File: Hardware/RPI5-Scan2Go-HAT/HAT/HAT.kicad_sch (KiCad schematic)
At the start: 30 parts, among them J1 RPi_GPIO, J10 Conn_01x02_Socket, J12 Conn_01x02_Socket, J13 Conn_01x02_Socket, J14 Conn_01x02_Socket, J15 Jack-DC 5V, J18 Conn_01x02_Socket, J19 Conn_01x02_Socket, J2 Conn_01x04_Socket, J20 Conn_01x05_Socket, J21 Conn_01x05_Socket, J22 Conn_01x02_Socket, J23 Conn_01x04_Socket, J24 Conn_01x02_Socket, J3 Conn_01x14_Socket, J4 Conn_01x03_Socket, J5 Conn_01x03_Socket, J6 Conn_01x03_Socket, J7 Conn_01x04_Socket, J8 Conn_01x02_Socket, J9 Conn_01x02_Socket, Q1 DMG2305UX, U1 Pico

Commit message: improved layout
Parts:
- renumbered J3 to J1, J24 to J10, J9 to J11, J15 to J12, J12 to J13, J13 to J14, J14 to J15, J18 to J16, J20 to J17, J2 to J18, J21 to J19, J1 to J2, J8 to J20, J19 to J21, J23 to J3, J10 to J8, J22 to J9

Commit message: started routing
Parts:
- renumbered J2 to J1, J8 to J10, J13 to J12, J14 to J13, J15 to J14, J12 to J15, J16 to J18, J21 to J19, J18 to J2, J17 to J20, J19 to J21, J9 to J22, J3 to J23, J10 to J24, J1 to J3, J20 to J8, J11 to J9

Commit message: removed 5V from barel to pi and pico
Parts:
- removed Q1: DMG2305UX, Package_TO_SOT_SMD:SOT-23, symbol Transistor_FET:DMG2301L
- F1: value 6A -> 10 A
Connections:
- net +5V: no longer D2.1 (VDD), J1.2 (5V), J1.4 (5V), J23.4 (Pin_4), J7.4 (Pin_4)
- net GND: now also J21.4 (Pin_4)
- net at U1.36 (3V3): no longer J21.4 (Pin_4)
- net VBUS: now reaches U1.40 (VBUS)
- net VBUS: now also D2.1 (VDD), J23.4 (Pin_4), J7.4 (Pin_4)
- no-connect marks 38 -> 42
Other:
- moved on the sheet: J21

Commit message: V0.1 of pcb finished (To be reviewed)
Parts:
- added H1, H2, H3, H4: MountingHole, symbol Mechanical:MountingHole
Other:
- moved on the sheet: D1, F1, J15, J21

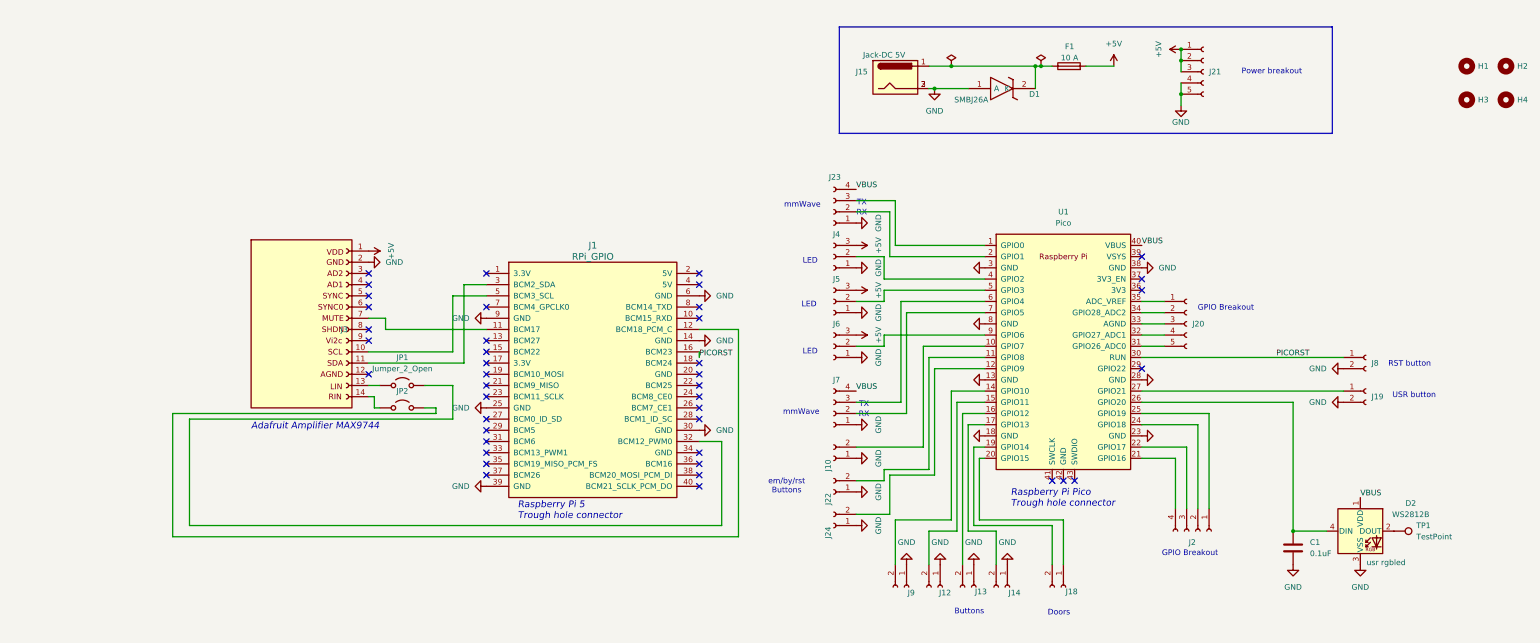
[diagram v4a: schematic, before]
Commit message: Silkscreen improvements and additions
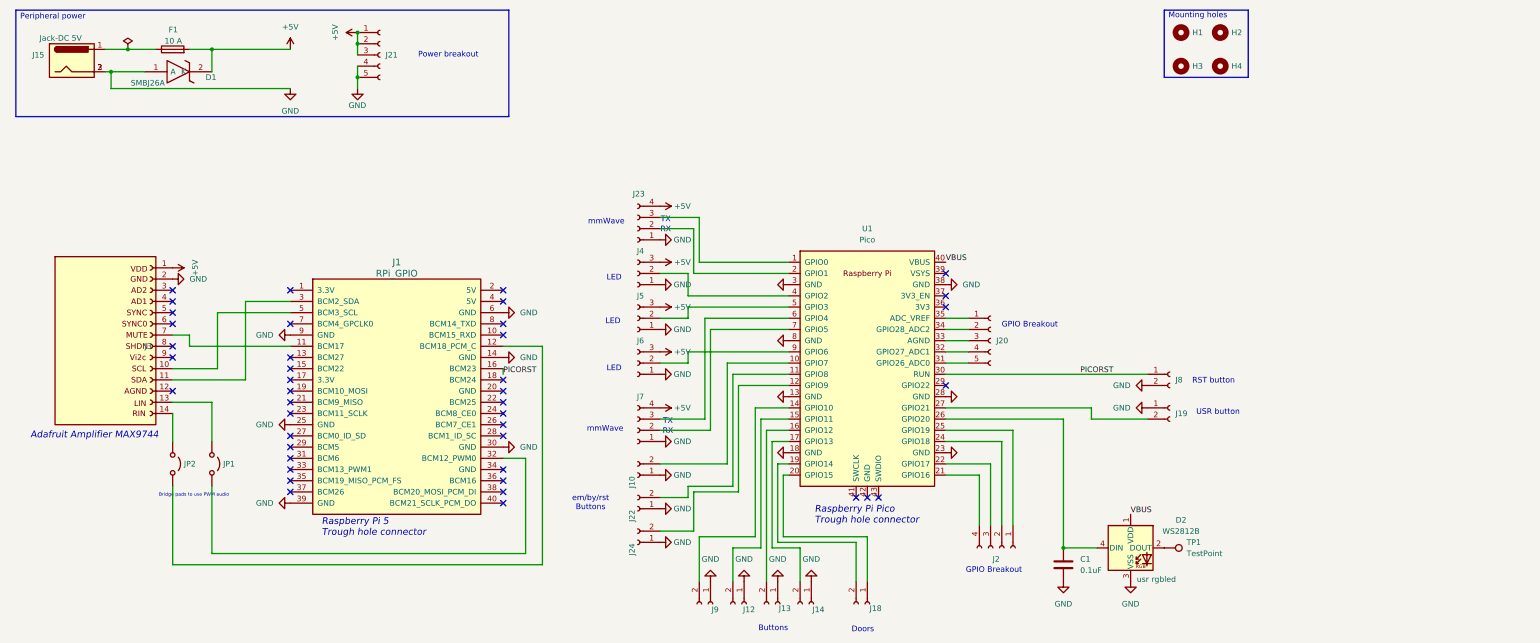
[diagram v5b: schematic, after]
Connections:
- net +5V: now also D1.2 (K), J23.4 (Pin_4), J7.4 (Pin_4)
- net GND: now also J19.1 (Pin_1); no longer J19.2 (Pin_2)
- net VBUS: no longer J23.4 (Pin_4), J7.4 (Pin_4)
- net at U1.27 (GPIO21): now also J19.2 (Pin_2); no longer J19.1 (Pin_1)
- net at F1.1, J15.1: no longer D1.2 (K)
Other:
- note added: "Bridge pads to use PWM audio"
- note added: "Mounting holes"
- note added: "Peripheral power"
- company: Casper R. Tak -> UMC Utrecht
- title: Scan2Go RPI-HAT -> Scan2Go FDS-HAT
- moved on the sheet: C1, D1, D2, F1, H1, H2, H3, H4, J1, J10, J12, J13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

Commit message: minor improvements
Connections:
- net GND: now also J8.1 (Pin_1); no longer J8.2 (Pin_2)
- net PICORST: now also J8.2 (Pin_2); no longer J8.1 (Pin_1)
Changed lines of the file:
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@@
+	(wire
+		(pts
+			(xy 241.3 95.25) (xy 241.3 97.79)
+		)
+		(stroke
+			(width 0)
+			(type default)
+		)
+	)
 	(wire
 		(pts
@@
 	(wire
 		(pts
-			(xy 223.52 95.25) (xy 269.24 95.25)
-		)
-		(stroke
-			(width 0)
-			(type default)
-		)
-	)
-	(wire
-		(pts
 			(xy 166.37 62.23) (xy 166.37 72.39)
 		)
@@
 	(wire
 		(pts
+			(xy 223.52 95.25) (xy 241.3 95.25)
+		)
+		(stroke
+			(width 0)
+			(type default)
+		)
+	)
+	(wire
+		(pts
 			(xy 176.53 121.92) (xy 176.53 97.79)
 		)
@@
 		(pts
 			(xy 223.52 87.63) (xy 228.6 87.63)
+		)
+		(stroke
+			(width 0)
+			(type default)
+		)
+	)
+	(wire
+		(pts
+			(xy 241.3 97.79) (xy 269.24 97.79)
 		)
 		(stroke
@@
 	)
 	(label "PICORST"
-		(at 254 95.25 0)
+		(at 251.46 97.79 0)
 		(fields_autoplaced yes)
 		(effects
@@
 	(symbol
 		(lib_id "power:GND")
-		(at 269.24 97.79 270)
+		(at 269.24 95.25 270)
 		(unit 1)
 		(exclude_from_sim no)
@@
 		(fields_autoplaced yes)
 		(property "Reference" "#PWR029"
-			(at 262.89 97.79 0)
+			(at 262.89 95.25 0)
 			(effects
 				(font
@@
 		)
 		(property "Value" "GND"
-			(at 265.43 97.7899 90)
+			(at 265.43 95.2499 90)
 			(effects
 				(font
@@
 		)
 		(property "Footprint" ""
-			(at 269.24 97.79 0)
+			(at 269.24 95.25 0)
 			(effects
 				(font
@@
 		)
 		(property "Datasheet" ""
-			(at 269.24 97.79 0)
+			(at 269.24 95.25 0)
 			(effects
 				(font
@@
 		)
 		(property "Description" "Power symbol creates a global label with name \"GND\" , ground"
-			(at 269.24 97.79 0)
-			(effects
-				(font
+			(at 269.24 95.25 0)
+			(effects
+				(font

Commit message: cleanup and added BOM
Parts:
- C1: Mouser (none) -> 581-12066D104KAT4A
- D1: value SMBJ26A -> c; Mouser (none) -> 652-SMBJ26A; Mouser Part Number 652-SMBJ26A -> (none)
- D2: Mouser (none) -> 474-COM-16346
- F1: Mouser (none) -> 652-SF-1206HH1000R-2
- H1, H2, H3, H4: footprint (none) -> MountingHole:MountingHole_3.2mm_M3
- J1: Mouser (none) -> 474-PRT-14017
- J10, J12, J13, J14, J18, J19, J22, J24, J8, J9: Farnell (none) -> 2399159
- J2, J23, J7: Farnell (none) -> 1830714
- J20, J21: Farnell (none) -> 1830716
- J3: Conrad (none) -> 2389174 - 62
- J4, J5, J6: Farnell (none) -> 2399161
- U1: Mouser (none) -> 358-SC0915
